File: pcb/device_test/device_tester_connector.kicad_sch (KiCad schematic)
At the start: 8 parts, among them J201 Conn_01x05, J202 USB_C_Receptacle_USB2.0_16P, J203 Conn_01x04, J204 Conn_01x08

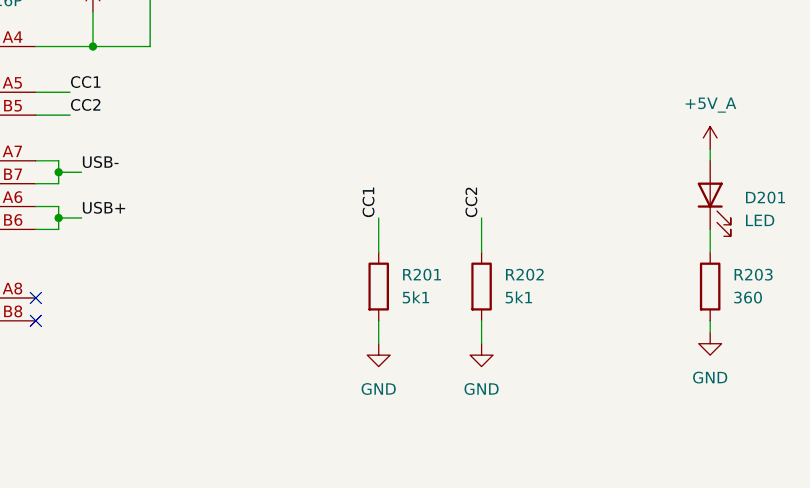
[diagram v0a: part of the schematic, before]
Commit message: remove usb a, add usb c
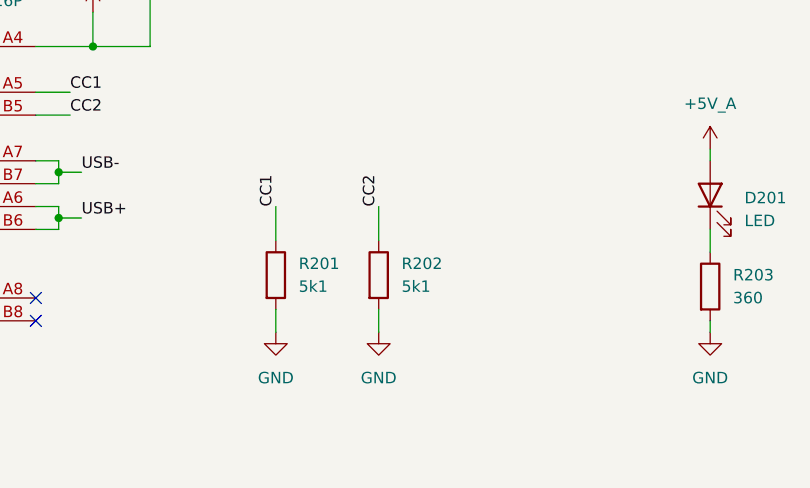
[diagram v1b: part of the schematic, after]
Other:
- moved on the sheet: R201, R202
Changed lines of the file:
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@@
 	(wire
 		(pts
-			(xy 175.26 90.17) (xy 175.26 93.98)
+			(xy 163.83 88.9) (xy 163.83 92.71)
 		)
 		(stroke
@@
 	(wire
 		(pts
-			(xy 175.26 101.6) (xy 175.26 104.14)
+			(xy 163.83 100.33) (xy 163.83 102.87)
 		)
 		(stroke
@@
 	(wire
 		(pts
-			(xy 163.83 90.17) (xy 163.83 93.98)
+			(xy 152.4 88.9) (xy 152.4 92.71)
 		)
 		(stroke
@@
 	(wire
 		(pts
-			(xy 163.83 101.6) (xy 163.83 104.14)
+			(xy 152.4 100.33) (xy 152.4 102.87)
 		)
 		(stroke
@@
 	)
 	(label "CC2"
-		(at 175.26 90.17 90)
+		(at 163.83 88.9 90)
 		(fields_autoplaced yes)
 		(effects
@@
 	)
 	(label "CC1"
-		(at 163.83 90.17 90)
+		(at 152.4 88.9 90)
 		(fields_autoplaced yes)
 		(effects
@@
 	(symbol
 		(lib_id "power:GND")
-		(at 175.26 104.14 0)
+		(at 163.83 102.87 0)
 		(unit 1)
 		(exclude_from_sim no)
@@
 		(fields_autoplaced yes)
 		(property "Reference" "#PWR0206"
-			(at 175.26 110.49 0)
+			(at 163.83 109.22 0)
 			(effects
 				(font
@@
 		)
 		(property "Value" "GND"
-			(at 175.26 109.22 0)
+			(at 163.83 107.95 0)
 			(effects
 				(font
@@
 		)
 		(property "Footprint" ""
-			(at 175.26 104.14 0)
+			(at 163.83 102.87 0)
 			(effects
 				(font
@@
 		)
 		(property "Datasheet" ""
-			(at 175.26 104.14 0)
+			(at 163.83 102.87 0)
 			(effects
 				(font
@@
 		)
 		(property "Description" "Power symbol creates a global label with name \"GND\" , ground"
-			(at 175.26 104.14 0)
+			(at 163.83 102.87 0)
 			(effects
 				(font
@@
 	(symbol
 		(lib_id "power:GND")
-		(at 163.83 104.14 0)
+		(at 152.4 102.87 0)
 		(unit 1)
 		(exclude_from_sim no)
@@
 		(fields_autoplaced yes)
 		(property "Reference" "#PWR0205"
-			(at 163.83 110.49 0)
+			(at 152.4 109.22 0)
 			(effects
 				(font
@@
 		)
 		(property "Value" "GND"
-			(at 163.83 109.22 0)
+			(at 152.4 107.95 0)
 			(effects
 				(font
@@
 		)
 		(property "Footprint" ""
-			(at 163.83 104.14 0)
+			(at 152.4 102.87 0)
 			(effects
 				(font
@@
 		)
 		(property "Datasheet" ""
-			(at 163.83 104.14 0)
+			(at 152.4 102.87 0)
 			(effects
 				(font
@@
 		)
 		(property "Description" "Power symbol creates a global label with name \"GND\" , ground"
-			(at 163.83 104.14 0)
+			(at 152.4 102.87 0)
 			(effects
 				(font
@@
 	(symbol
 		(lib_id "Device:R")
-		(at 163.83 97.79 0)
+		(at 152.4 96.52 0)
 		(unit 1)
 		(exclude_from_sim no)
@@
 		(fields_autoplaced yes)
 		(property "Reference" "R201"
-			(at 166.37 96.5199 0)
+			(at 154.94 95.2499 0)
 			(effects
 				(font
@@
 		)
 		(property "Value" "5k1"
-			(at 166.37 99.0599 0)
+			(at 154.94 97.7899 0)
 			(effects
 				(font
@@
 		)
 		(property "Footprint" "Resistor_SMD:R_0805_2012Metric"
-			(at 162.052 97.79 90)
+			(at 150.622 96.52 90)
 			(effects
 				(font
@@
 		)
 		(property "Datasheet" "~"
-			(at 163.83 97.79 0)
+			(at 152.4 96.52 0)
 			(effects
 				(font
@@
 		)
 		(property "Description" "Resistor"
-			(at 163.83 97.79 0)
+			(at 152.4 96.52 0)
 			(effects
 				(font
@@
 		)
 		(property "LCSC" ""
-			(at 163.83 97.79 0)
+			(at 152.4 96.52 0)
 			(effects
 				(font
@@
 	(symbol
 		(lib_id "Device:R")
-		(at 175.26 97.79 0)
+		(at 163.83 96.52 0)
 		(unit 1)
 		(exclude_from_sim no)
@@
 		(fields_autoplaced yes)
 		(property "Reference" "R202"
-			(at 177.8 96.5199 0)
+			(at 166.37 95.2499 0)
 			(effects
 				(font
@@
 		)
 		(property "Value" "5k1"
-			(at 177.8 99.0599 0)
+			(at 166.37 97.7899 0)
 			(effects
 				(font
@@
 		)
 		(property "Footprint" "Resistor_SMD:R_0805_2012Metric"
-			(at 173.482 97.79 90)
+			(at 162.052 96.52 90)
 			(effects
 				(font
@@
 		)
 		(property "Datasheet" "~"
-			(at 175.26 97.79 0)
+			(at 163.83 96.52 0)
 			(effects
 				(font
@@
 		)
 		(property "Description" "Resistor"
-			(at 175.26 97.79 0)
+			(at 163.83 96.52 0)
 			(effects
 				(font
@@
 		)
 		(property "LCSC" ""
-			(at 175.26 97.79 0)
-			(effects
-				(font
+			(at 163.83 96.52 0)
+			(effects
+				(font

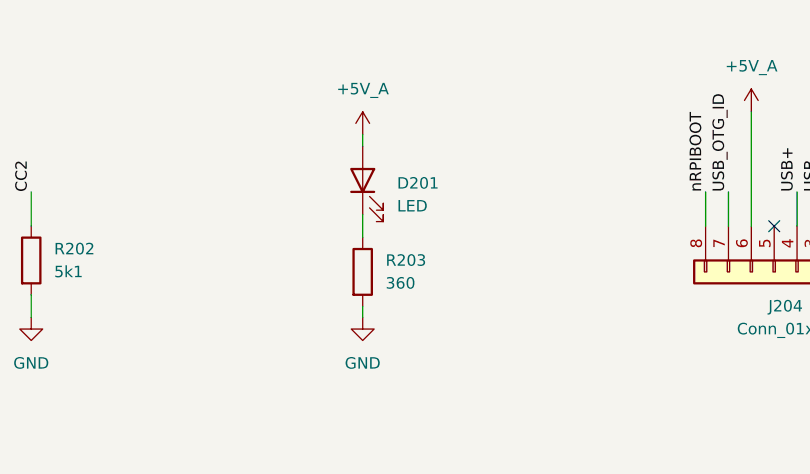
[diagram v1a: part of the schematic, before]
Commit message: update LCSC codes
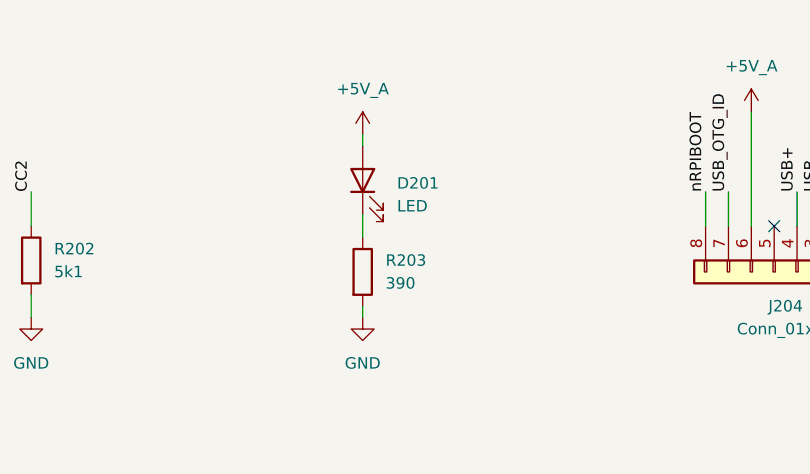
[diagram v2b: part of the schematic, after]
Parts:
- D201: LCSC (none) -> C84256
- J203: LCSC (none) -> C2691448
- R201, R202: LCSC (none) -> C27834
- R203: value 360 -> 390; LCSC (none) -> C17655
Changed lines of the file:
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@@
 			)
 		)
-		(property "LCSC" ""
+		(property "LCSC" "C84256"
 			(at 200.66 87.63 0)
 			(effects
@@
 			)
 		)
-		(property "LCSC" ""
+		(property "LCSC" "C27834"
 			(at 152.4 96.52 0)
 			(effects
@@
 			)
 		)
-		(property "LCSC" ""
+		(property "LCSC" "C27834"
 			(at 163.83 96.52 0)
 			(effects
@@
 			)
 		)
-		(property "Value" "360"
+		(property "Value" "390"
 			(at 203.2 99.0599 0)
 			(effects
@@
 			)
 		)
-		(property "LCSC" ""
+		(property "LCSC" "C17655"
 			(at 200.66 97.79 0)
 			(effects
@@
 			(at 234.95 39.37 0)
 			(effects
+				(font
+					(size 1.27 1.27)
+				)
+				(hide yes)
+			)
+		)
+		(property "LCSC" "C2691448"
+			(at 234.95 39.37 0)
+			(effects

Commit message: update device test pcb
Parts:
- removed J201: Conn_01x05, Connector_PinSocket_2.54mm:PinSocket_1x05_P2.54mm_Horizontal, symbol Connector_Generic:Conn_01x05
- removed J204: Conn_01x08, Connector_PinSocket_2.54mm:PinSocket_1x08_P2.54mm_Horizontal, symbol Connector_Generic:Conn_01x08
- added J203: Conn_02x10_Row_Letter_First, Connector_DIN:DIN41612_B3_2x10_Male_Horizontal_THT, symbol Connector_Generic:Conn_02x10_Row_Letter_First
- renumbered J202 to J201, J203 to J202
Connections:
- net +12V: now also J203.a1 (Pin_a1), J203.a2 (Pin_a2), J203.b1 (Pin_b1), J203.b2 (Pin_b2)
- net +5V_A: now also J203.a4 (Pin_a4), J203.a5 (Pin_a5), J203.b4 (Pin_b4), J203.b5 (Pin_b5)
- net GND: now also J203.a10 (Pin_a10), J203.a3 (Pin_a3), J203.b10 (Pin_b10), J203.b3 (Pin_b3)
- net USB+: now also J203.a6 (Pin_a6)
- net USB-: now also J203.b6 (Pin_b6)
- net USB_OTG_ID: now also J203.a8 (Pin_a8)
- net nRPIBOOT: now also J203.a9 (Pin_a9)
- no-connect marks 5 -> 6
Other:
- moved on the sheet: D201, J201, J202, R201, R202, R203

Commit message: update footprints and step's
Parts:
- J203: footprint Connector_DIN:DIN41612_B3_2x10_Male_Horizontal_THT -> USB:PCN10C-20S-2.54DS
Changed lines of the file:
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@@
 	(label "nRPIBOOT"
 		(at 185.42 109.22 180)
-		(fields_autoplaced yes)
 		(effects
 			(font
@@
 	(label "USB-"
 		(at 106.68 96.52 0)
-		(fields_autoplaced yes)
 		(effects
 			(font
@@
 	(label "nRPIBOOT"
 		(at 144.78 68.58 270)
-		(fields_autoplaced yes)
 		(effects
 			(font
@@
 	(label "CC1"
 		(at 105.41 87.63 0)
-		(fields_autoplaced yes)
 		(effects
 			(font
@@
 	(label "CC2"
 		(at 139.7 100.33 90)
-		(fields_autoplaced yes)
 		(effects
 			(font
@@
 	(label "CC1"
 		(at 128.27 100.33 90)
-		(fields_autoplaced yes)
 		(effects
 			(font
@@
 	(label "USB+"
 		(at 106.68 101.6 0)
-		(fields_autoplaced yes)
 		(effects
 			(font
@@
 	(label "CC2"
 		(at 105.41 90.17 0)
-		(fields_autoplaced yes)
 		(effects
 			(font
@@
 	(label "USB-"
 		(at 210.82 101.6 0)
-		(fields_autoplaced yes)
 		(effects
 			(font
@@
 	(label "USB+"
 		(at 185.42 101.6 180)
-		(fields_autoplaced yes)
 		(effects
 			(font
@@
 	(label "USB_OTG_ID"
 		(at 185.42 106.68 180)
-		(fields_autoplaced yes)
 		(effects
 			(font
@@
 	(label "USB_OTG_ID"
 		(at 147.32 68.58 270)
-		(fields_autoplaced yes)
 		(effects
 			(font
@@
 			)
 		)
-		(property "Footprint" "Connector_DIN:DIN41612_B3_2x10_Male_Horizontal_THT"
+		(property "Footprint" "USB:PCN10C-20S-2.54DS"
 			(at 196.85 99.06 0)
 			(effects

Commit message: update footprint lib name & change connector footprint
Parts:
- J203: footprint USB:PCN10C-20S-2.54DS -> PRJ:PCN10-20P-2.54DS
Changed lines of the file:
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@@
 			)
 		)
-		(property "Footprint" "USB:PCN10C-20S-2.54DS"
+		(property "Footprint" "PRJ:PCN10-20P-2.54DS"
 			(at 196.85 99.06 0)
 			(effects

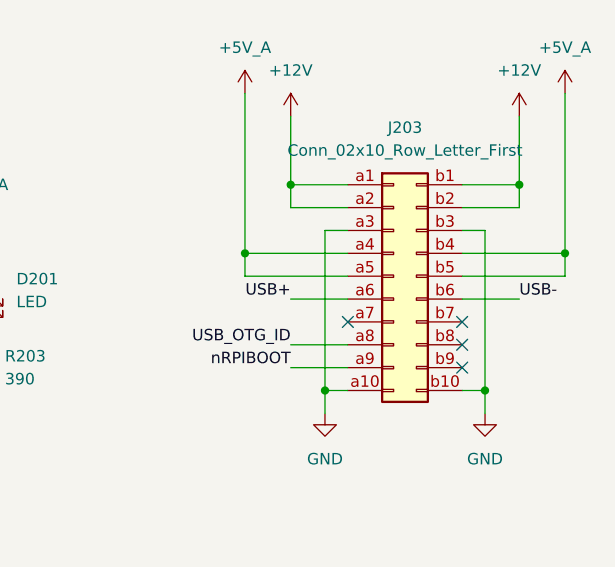
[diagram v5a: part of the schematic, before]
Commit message: fix pin assignment
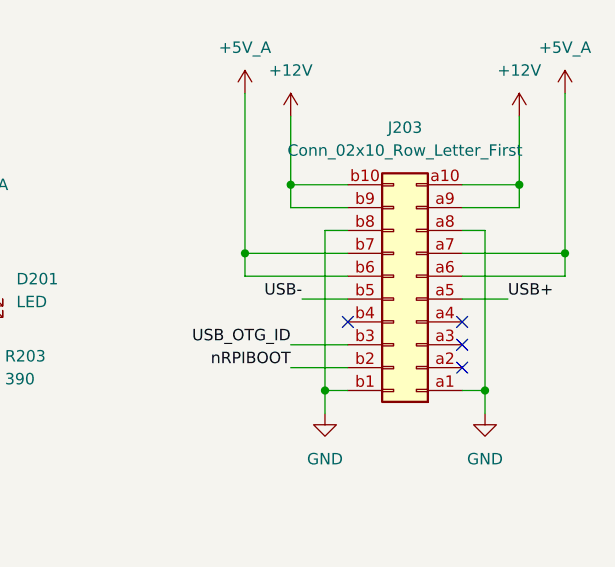
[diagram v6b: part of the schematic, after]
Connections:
- net +12V: now also J203.a10 (Pin_a10), J203.a9 (Pin_a9), J203.b10 (Pin_b10), J203.b9 (Pin_b9); no longer J203.a1 (Pin_a1), J203.a2 (Pin_a2), J203.b1 (Pin_b1), J203.b2 (Pin_b2)
- net +5V_A: now also J203.a6 (Pin_a6), J203.a7 (Pin_a7), J203.b6 (Pin_b6), J203.b7 (Pin_b7); no longer J203.a4 (Pin_a4), J203.a5 (Pin_a5), J203.b4 (Pin_b4), J203.b5 (Pin_b5)
- net GND: now also J203.a1 (Pin_a1), J203.a8 (Pin_a8), J203.b1 (Pin_b1), J203.b8 (Pin_b8); no longer J203.a10 (Pin_a10), J203.a3 (Pin_a3), J203.b10 (Pin_b10), J203.b3 (Pin_b3)
- net USB+: now also J203.a5 (Pin_a5); no longer J203.a6 (Pin_a6)
- net USB-: now also J203.b5 (Pin_b5); no longer J203.b6 (Pin_b6)
- net USB_OTG_ID: now also J203.b3 (Pin_b3); no longer J203.a8 (Pin_a8)
- net nRPIBOOT: now also J203.b2 (Pin_b2); no longer J203.a9 (Pin_a9)
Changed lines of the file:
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@@
+	(wire
+		(pts
+			(xy 186.69 101.6) (xy 191.77 101.6)
+		)
+		(stroke
+			(width 0)
+			(type default)
+		)
+	)
 	(wire
 		(pts
@@
 	(wire
 		(pts
-			(xy 185.42 101.6) (xy 191.77 101.6)
-		)
-		(stroke
-			(width 0)
-			(type default)
-		)
-	)
-	(wire
-		(pts
 			(xy 78.74 120.65) (xy 78.74 121.92)
 		)
@@
 	(wire
 		(pts
+			(xy 204.47 101.6) (xy 209.55 101.6)
+		)
+		(stroke
+			(width 0)
+			(type default)
+		)
+	)
+	(wire
+		(pts
 			(xy 151.13 113.03) (xy 151.13 114.3)
 		)
@@
 		(pts
 			(xy 204.47 93.98) (xy 207.01 93.98)
-		)
-		(stroke
-			(width 0)
-			(type default)
-		)
-	)
-	(wire
-		(pts
-			(xy 204.47 101.6) (xy 210.82 101.6)
 		)
 		(stroke
@@
 	)
 	(label "USB-"
-		(at 210.82 101.6 0)
+		(at 186.69 101.6 180)
 		(effects
 			(font
 				(size 1.27 1.27)
 			)
-			(justify left bottom)
+			(justify right bottom)
 		)
 	)
 	(label "USB+"
-		(at 185.42 101.6 180)
+		(at 209.55 101.6 0)
 		(effects
 			(font
 				(size 1.27 1.27)
 			)
-			(justify right bottom)
+			(justify left bottom)
 		)
 	)
@@
 	)
 	(symbol
-		(lib_id "Connector_Generic:Conn_02x10_Row_Letter_First")
-		(at 196.85 99.06 0)
-		(unit 1)
-		(exclude_from_sim no)
-		(in_bom yes)
-		(on_board yes)
-		(dnp no)
-		(fields_autoplaced yes)
-		(property "Reference" "J203"
-			(at 198.12 82.55 0)
-			(effects
-				(font
-					(size 1.27 1.27)
-				)
-			)
-		)
-		(property "Value" "Conn_02x10_Row_Letter_First"
-			(at 198.12 85.09 0)
-			(effects
-				(font
-					(size 1.27 1.27)
-				)
-			)
-		)
-		(property "Footprint" "PRJ:PCN10-20P-2.54DS"
-			(at 196.85 99.06 0)
-			(effects
-				(font
-					(size 1.27 1.27)
-				)
-				(hide yes)
-			)
-		)
-		(property "Datasheet" "~"
-			(at 196.85 99.06 0)
-			(effects
-				(font
-					(size 1.27 1.27)
-				)
-				(hide yes)
-			)
-		)
-		(property "Description" "Generic connector, double row, 02x10, row letter first pin numbering scheme (pin number consists of a letter for the row and a number for the pin index in this row. a1, ..., aN; b1, ..., bN), script generated (kicad-library-utils/schlib/autogen/connector/)"
-			(at 196.85 99.06 0)
-			(effects
-				(font
-					(size 1.27 1.27)
-				)
-				(hide yes)
-			)
-		)
-		(property "LCSC" ""
-			(at 196.85 99.06 0)
-			(effects
-				(font
-					(size 1.27 1.27)
-				)
-				(hide yes)
-			)
-		)
-		(pin "a5"
-		)
-		(pin "a6"
-		)
-		(pin "a7"
-		)
-		(pin "a8"
-		)
-		(pin "a9"
-		)
-		(pin "b1"
-		)
-		(pin "b10"
-		)
-		(pin "b2"
-		)
-		(pin "b3"
-		)
-		(pin "a4"
-		)
-		(pin "b8"
-		)
-		(pin "b9"
-		)
-		(pin "a3"
-		)
-		(pin "b4"
-		)
-		(pin "b5"
-		)
-		(pin "b7"
-		)
-		(pin "b6"
-		)
-		(pin "a1"
-		)
-		(pin "a2"
-		)
-		(pin "a10"
-		)
-		(instances
-			(project ""
-				(path "/5d20b266-567e-45c6-9e3e-145c2aea1daa/35b99cfb-c0ef-4b54-9d41-3482303768a8"
-					(reference "J203")
-					(unit 1)
-				)
-			)
-		)
-	)
-	(symbol
 		(lib_id "Device:LED")
 		(at 151.13 99.06 90)
@@
 					(unit 1)
 				)
+			)
+		)
+	)
+	(symbol
+		(lib_id "Connector_Generic:Conn_02x10_Row_Letter_First")
+		(at 199.39 101.6 180)
+		(unit 1)
+		(exclude_from_sim no)
+		(in_bom yes)
+		(on_board yes)
+		(dnp no)
+		(fields_autoplaced yes)
+		(property "Reference" "J203"
+			(at 198.12 82.55 0)
+			(effects
+				(font
+					(size 1.27 1.27)
+				)
+			)
+		)
+		(property "Value" "Conn_02x10_Row_Letter_First"
+			(at 198.12 85.09 0)
+			(effects
+				(font
+					(size 1.27 1.27)
+				)
+			)
+		)
+		(property "Footprint" "PRJ:PCN10-20P-2.54DS"
+			(at 199.39 101.6 0)
+			(effects
+				(font
+					(size 1.27 1.27)
+				)
+				(hide yes)
+			)
+		)
+		(property "Datasheet" "~"
+			(at 199.39 101.6 0)
+			(effects
+				(font
+					(size 1.27 1.27)
+				)
+				(hide yes)
+			)
+		)
+		(property "Description" "Generic connector, double row, 02x10, row letter first pin numbering scheme (pin number consists of a letter for the row and a number for the pin index in this row. a1, ..., aN; b1, ..., bN), script generated (kicad-library-utils/schlib/autogen/connector/)"
+			(at 199.39 101.6 0)
+			(effects
+				(font
+					(size 1.27 1.27)
+				)
+				(hide yes)
+			)
+		)
+		(property "LCSC" ""
+			(at 199.39 101.6 0)
+			(effects
+				(font
+					(size 1.27 1.27)
+				)
+				(hide yes)
+			)
+		)
+		(pin "a3"
+		)
+		(pin "a10"
+		)
+		(pin "a4"
+		)
+		(pin "b2"
+		)
+		(pin "b3"
+		)
+		(pin "b4"
+		)
+		(pin "a2"
+		)
+		(pin "b5"
+		)
+		(pin "a5"
+		)
+		(pin "b6"
+		)
+		(pin "b1"
+		)
+		(pin "a1"
+		)
+		(pin "a9"
+		)
+		(pin "a8"
+		)
+		(pin "b8"
+		)
+		(pin "b9"
+		)
+		(pin "b10"
+		)
+		(pin "a7"
+		)
+		(pin "b7"
+		)
+		(pin "a6"
+		)
+		(instances
+			(project ""
+				(path "/5d20b266-567e-45c6-9e3e-145c2aea1daa/35b99cfb-c0ef-4b54-9d41-3482303768a8"
+					(reference "J203")
+					(unit 1)
+				)

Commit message: update
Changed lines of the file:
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@@
 	(wire
 		(pts
-			(xy 144.78 63.5) (xy 144.78 68.58)
+			(xy 144.78 63.5) (xy 144.78 77.47)
 		)
 		(stroke
@@
 	(wire
 		(pts
-			(xy 104.14 101.6) (xy 106.68 101.6)
+			(xy 104.14 101.6) (xy 111.76 101.6)
 		)
 		(stroke
@@
 	(wire
 		(pts
-			(xy 186.69 101.6) (xy 191.77 101.6)
+			(xy 175.26 101.6) (xy 191.77 101.6)
 		)
 		(stroke
@@
 	(wire
 		(pts
-			(xy 101.6 87.63) (xy 105.41 87.63)
+			(xy 101.6 87.63) (xy 107.95 87.63)
 		)
 		(stroke
@@
 	(wire
 		(pts
-			(xy 204.47 101.6) (xy 209.55 101.6)
+			(xy 204.47 101.6) (xy 217.17 101.6)
 		)
 		(stroke
@@
 	(wire
 		(pts
-			(xy 104.14 96.52) (xy 106.68 96.52)
+			(xy 104.14 96.52) (xy 111.76 96.52)
 		)
 		(stroke
@@
 	(wire
 		(pts
-			(xy 139.7 100.33) (xy 139.7 104.14)
+			(xy 139.7 97.79) (xy 139.7 104.14)
 		)
 		(stroke
@@
 	(wire
 		(pts
-			(xy 101.6 90.17) (xy 105.41 90.17)
+			(xy 101.6 90.17) (xy 107.95 90.17)
 		)
 		(stroke
@@
 	(wire
 		(pts
-			(xy 185.42 109.22) (xy 191.77 109.22)
+			(xy 175.26 109.22) (xy 191.77 109.22)
 		)
 		(stroke
@@
 	(wire
 		(pts
-			(xy 185.42 106.68) (xy 191.77 106.68)
+			(xy 175.26 106.68) (xy 191.77 106.68)
 		)
 		(stroke
@@
 	(wire
 		(pts
-			(xy 147.32 63.5) (xy 147.32 68.58)
+			(xy 147.32 63.5) (xy 147.32 77.47)
 		)
 		(stroke
@@
 	(wire
 		(pts
-			(xy 128.27 100.33) (xy 128.27 104.14)
+			(xy 128.27 97.79) (xy 128.27 104.14)
 		)
 		(stroke
@@
 	)
 	(label "nRPIBOOT"
-		(at 185.42 109.22 180)
+		(at 175.26 109.22 0)
+		(effects
+			(font
+				(size 1.27 1.27)
+			)
+			(justify left bottom)
+		)
+	)
+	(label "USB-"
+		(at 111.76 96.52 180)
 		(effects
 			(font
@@
 		)
 	)
+	(label "nRPIBOOT"
+		(at 144.78 77.47 90)
+		(effects
+			(font
+				(size 1.27 1.27)
+			)
+			(justify left bottom)
+		)
+	)
+	(label "CC1"
+		(at 107.95 87.63 180)
+		(effects
+			(font
+				(size 1.27 1.27)
+			)
+			(justify right bottom)
+		)
+	)
+	(label "CC2"
+		(at 139.7 97.79 270)
+		(effects
+			(font
+				(size 1.27 1.27)
+			)
+			(justify right bottom)
+		)
+	)
+	(label "CC1"
+		(at 128.27 97.79 270)
+		(effects
+			(font
+				(size 1.27 1.27)
+			)
+			(justify right bottom)
+		)
+	)
+	(label "USB+"
+		(at 111.76 101.6 180)
+		(effects
+			(font
+				(size 1.27 1.27)
+			)
+			(justify right bottom)
+		)
+	)
+	(label "CC2"
+		(at 107.95 90.17 180)
+		(effects
+			(font
+				(size 1.27 1.27)
+			)
+			(justify right bottom)
+		)
+	)
 	(label "USB-"
-		(at 106.68 96.52 0)
+		(at 175.26 101.6 0)
 		(effects
 			(font
@@
 		)
 	)
-	(label "nRPIBOOT"
-		(at 144.78 68.58 270)
+	(label "USB+"
+		(at 217.17 101.6 180)
 		(effects
 			(font
@@
 		)
 	)
-	(label "CC1"
-		(at 105.41 87.63 0)
+	(label "USB_OTG_ID"
+		(at 175.26 106.68 0)
 		(effects
 			(font
@@
 		)
 	)
-	(label "CC2"
-		(at 139.7 100.33 90)
+	(label "USB_OTG_ID"
+		(at 147.32 77.47 90)
 		(effects
 			(font
@@
 		)
 	)
-	(label "CC1"
-		(at 128.27 100.33 90)
-		(effects
-			(font
-				(size 1.27 1.27)
-			)
-			(justify left bottom)
-		)
-	)
-	(label "USB+"
-		(at 106.68 101.6 0)
-		(effects
-			(font
-				(size 1.27 1.27)
-			)
-			(justify left bottom)
-		)
-	)
-	(label "CC2"
-		(at 105.41 90.17 0)
-		(effects
-			(font
-				(size 1.27 1.27)
-			)
-			(justify left bottom)
-		)
-	)
-	(label "USB-"
-		(at 186.69 101.6 180)
-		(effects
-			(font
-				(size 1.27 1.27)
-			)
-			(justify right bottom)
-		)
-	)
-	(label "USB+"
-		(at 209.55 101.6 0)
-		(effects
-			(font
-				(size 1.27 1.27)
-			)
-			(justify left bottom)
-		)
-	)
-	(label "USB_OTG_ID"
-		(at 185.42 106.68 180)
-		(effects
-			(font
-				(size 1.27 1.27)
-			)
-			(justify right bottom)
-		)
-	)
-	(label "USB_OTG_ID"
-		(at 147.32 68.58 270)
-		(effects
-			(font
-				(size 1.27 1.27)
-			)
-			(justify right bottom)
-		)
-	)

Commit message: add caps
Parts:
- added C201: 100u / 25V, Capacitor_Tantalum_SMD:CP_EIA-7343-43_Kemet-X_Pad2.25x2.55mm_HandSolder, symbol Device:C_Polarized
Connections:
- net +5V_A: now also C201.1
- net GND: now also C201.2
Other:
- moved on the sheet: J202
